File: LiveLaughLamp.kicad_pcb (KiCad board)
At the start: 2 copper layers, 120 x 20 mm, 46 parts, among them Q1 BSS138, SW1 1437566-3, U1 XIAO-ESP32-C3-SMD, U2 PCA9685BS, U3 PCA9306D

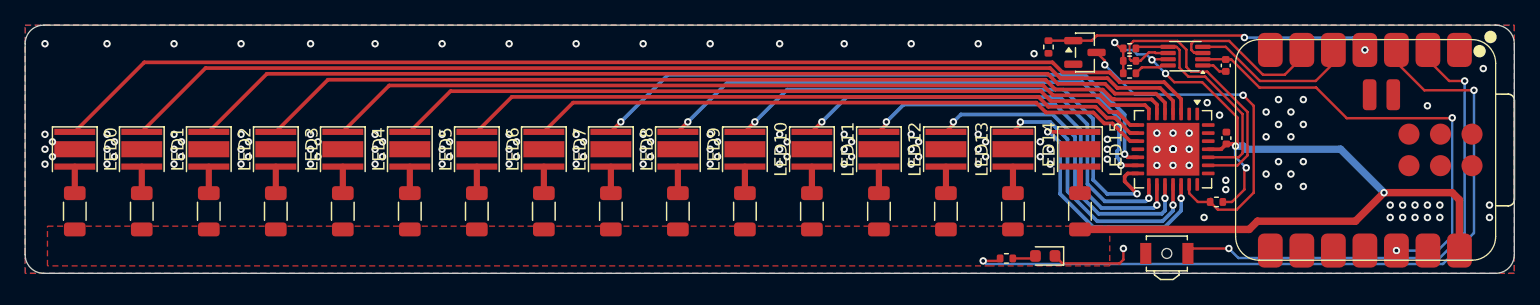
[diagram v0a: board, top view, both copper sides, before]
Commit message: Swap LED controller for TLC5971
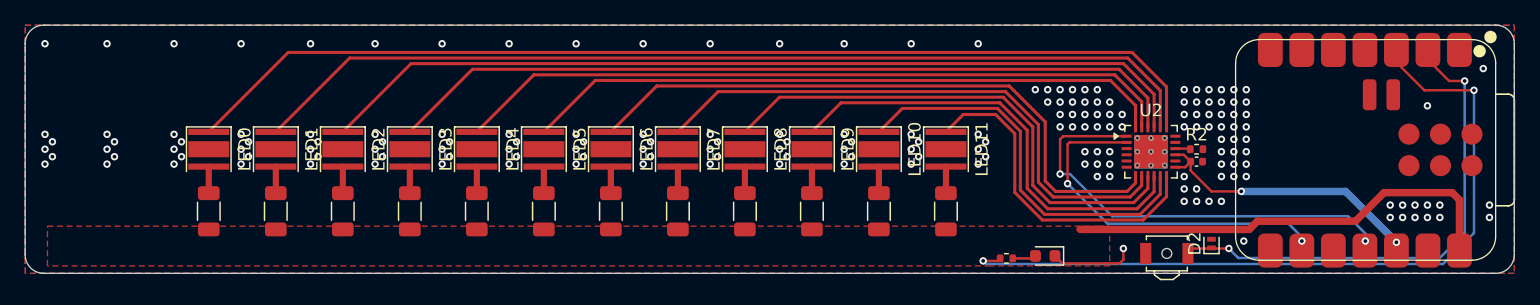
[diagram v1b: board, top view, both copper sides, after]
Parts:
- removed C2: 1µ, Capacitor_SMD:C_0402_1005Metric
- removed LED12, LED13, LED14, LED15: LED, LED_SMD:LED_Cree-XP-G
- removed Q1: BSS138, Package_TO_SOT_SMD:SOT-23
- removed R17, R20, R21: 200k, Resistor_SMD:R_0402_1005Metric
- removed R18, R19: 1k82, Resistor_SMD:R_0402_1005Metric
- removed RD12, RD13, RD14, RD15: R_US, Resistor_SMD:R_1206_3216Metric
- removed U3: PCA9306D, Package_SO:VSSOP-8_2.3x2mm_P0.5mm
- added D2: PESD3V3S1UL, Diode_SMD:D_SOD-882, F.Cu at (195.6, 117.6)
- added R2: 1k22 1%, Resistor_SMD:R_0402_1005Metric, F.Cu at (194.4, 110.0)
- R1: value 1k82 -> 1k22
- U2: value PCA9685BS -> TLC5971RGE; footprint Package_DFN_QFN:QFN-28-1EP_6x6mm_P0.65mm_EP4.25x4.25mm -> Package_DFN_QFN:Texas_RGE0024H_VQFN-24-1EP_4x4mm_P0.5mm_EP2.7x2.7mm_ThermalVias
- moved LED10 10.8 mm to (168.8, 110.0)
- moved LED4 10.8 mm to (136.4, 110.0)
- moved LED5 10.8 mm to (141.8, 110.0)
- moved LED8 10.8 mm to (158.0, 110.0)
- moved LED9 10.8 mm to (163.4, 110.0)
- moved RD10 10.8 mm to (168.8, 115.0)
- moved RD4 10.8 mm to (136.4, 115.0)
- moved RD5 10.8 mm to (141.8, 115.0)
- moved RD8 10.8 mm to (158.0, 115.0)
- moved RD9 10.8 mm to (163.4, 115.0)
- moved LED0 10.8 mm to (114.8, 110.0)
- moved LED1 10.8 mm to (120.2, 110.0)
- moved LED2 10.8 mm to (125.6, 110.0)
- moved LED3 10.8 mm to (131.0, 110.0)
- moved RD0 10.8 mm to (114.8, 115.0)
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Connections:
- C1 pad 2: +5V -> +3.3V
- LED0 pad 3: GND -> (no net)
- LED1 pad 3: GND -> (no net)
- LED10 pad 3: GND -> (no net)
- LED11 pad 3: GND -> (no net)
- LED2 pad 3: GND -> (no net)
- LED3 pad 3: GND -> (no net)
- LED4 pad 3: GND -> (no net)
- LED5 pad 3: GND -> (no net)
- LED6 pad 3: GND -> (no net)
- LED7 pad 3: GND -> (no net)
- LED8 pad 3: GND -> (no net)
- LED9 pad 3: GND -> (no net)
- U1 pad 11: unconnected-(U1-GPIO10_D10_MOSI-Pad11) -> /MOSI
- U1 pad 4: /OE_3V3 -> unconnected-(U1-GPIO5_A3_D3-Pad4)
- U1 pad 5: /SDA_3V3 -> unconnected-(U1-GPIO6_D4_SDA-Pad5)
- U1 pad 6: /SCL_3V3 -> unconnected-(U1-GPIO7_D5_SCL-Pad6)
- U1 pad 9: unconnected-(U1-GPIO8_D8_SCK-Pad9) -> /SCK
- U2 pad 1: GND -> /MOSI
- U2 pad 10: /LED array/LED7 -> /LED array/LED9
- U2 pad 11: GND -> /LED array/LED10
- U2 pad 12: /LED array/LED8 -> /LED array/LED11
- U2 pad 13: /LED array/LED9 -> +3.3V
- U2 pad 14: /LED array/LED10 -> unconnected-(U2-NC-Pad14)
- U2 pad 15: /LED array/LED11 -> +3.3V
- U2 pad 16: /LED array/LED12 -> Net-(U2-IREF)
- U2 pad 17: /LED array/LED13 -> unconnected-(U2-NC-Pad17)
- U2 pad 18: /LED array/LED14 -> GND
- U2 pad 19: /LED array/LED15 -> /LED array/LED0
- U2 pad 2: GND -> /SCK
- U2 pad 20: /~{OE_5V} -> /LED array/LED1
- U2 pad 21: GND -> /LED array/LED2
- U2 pad 22: GND -> /LED array/LED3
- U2 pad 23: /SCL_5V -> /LED array/LED4
- U2 pad 24: /SDA_5V -> /LED array/LED5
- U2 pad 25: +5V -> GND
- U2 pad 3: /LED array/LED0 -> unconnected-(U2-NC-Pad3)
- U2 pad 4: /LED array/LED1 -> unconnected-(U2-NC-Pad4)
- U2 pad 5: /LED array/LED2 -> unconnected-(U2-SCKO-Pad5)
- U2 pad 6: /LED array/LED3 -> unconnected-(U2-SDTO-Pad6)
- U2 pad 7: /LED array/LED4 -> /LED array/LED6
- U2 pad 8: /LED array/LED5 -> /LED array/LED7
- U2 pad 9: /LED array/LED6 -> /LED array/LED8
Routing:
- net +5V: track 77.2 -> 36.1 mm, vias 6 -> 0
- net /MOSI: track 0.00 -> 36.2 mm, vias 0 -> 2
- net /LED array/LED12: track 31.3 -> 0.00 mm, vias 2 -> 0
- net /SCK: track 0.00 -> 29.7 mm, vias 0 -> 2
- net /~{OE_5V}: track 28.7 -> 0.00 mm, vias 2 -> 0
- net /LED array/LED13: track 26.4 -> 0.00 mm, vias 2 -> 0
- net /OE_3V3: track 26.2 -> 0.00 mm, vias 2 -> 0
- net /SCL_5V: track 24.4 -> 0.00 mm
- net /LED array/LED15: track 21.6 -> 0.00 mm, vias 2 -> 0
- net /LED array/LED14: track 21.6 -> 0.00 mm, vias 2 -> 0
- net /SDA_5V: track 17.8 -> 0.00 mm
- net +3.3V: track 36.6 -> 22.6 mm
- net /SDA_3V3: track 13.3 -> 0.00 mm
- net /SCL_3V3: track 12.9 -> 0.00 mm
- net /LED array/LED10: track 42.4 -> 31.9 mm, vias 2 -> 0
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
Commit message: Add thermal sink for Xiao board. Add JLC fabrication metadata.
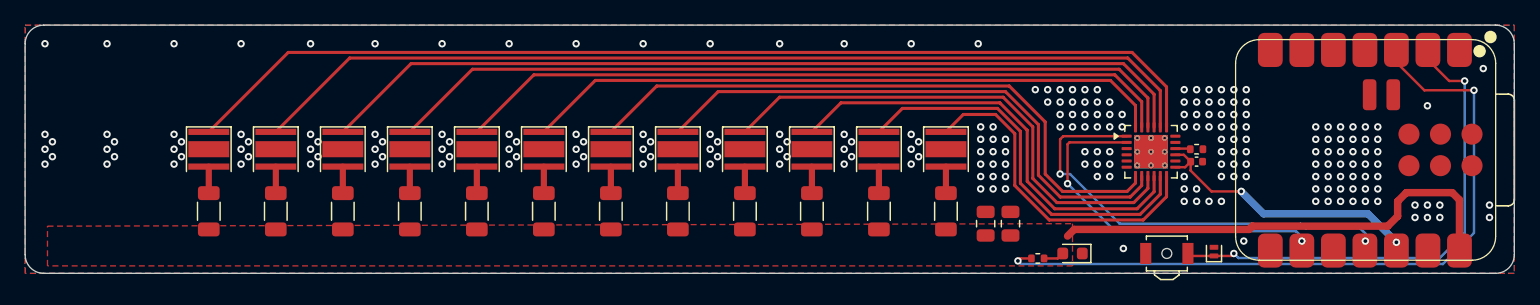
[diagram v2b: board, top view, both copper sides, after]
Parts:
- added C2: 22µ, Capacitor_SMD:C_0805_2012Metric, F.Cu at (177.4, 116.0)
- added C3: 22µ, Capacitor_SMD:C_0805_2012Metric, F.Cu at (179.4, 116.0)
- moved R1 2.53 mm to (181.6, 118.8)
- moved D1 2.21 mm to (184.4, 118.4)
- moved D2 0.68 mm to (195.8, 118.2)
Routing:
- net GND: track 7.07 -> 0.00 mm, vias 181 -> 231
- net /~{LED}: track 61.8 -> 58.7 mm
- net +5V: track 36.1 -> 38.1 mm
